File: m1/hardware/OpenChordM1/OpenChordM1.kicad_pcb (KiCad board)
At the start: 2 copper layers, 119 x 63.1 mm, 20 parts, among them J1 USB4105-GF-A, J2 SJ1-3523N, J3 SJ1-3523N, SW1 SW_Gateron_LP, SW10 EVQ-PUA02K, SW11 EVQ-PUA02K, SW2 SW_Gateron_LP, SW3 SW_Gateron_LP, SW4 SW_Gateron_LP, SW5 SW_Gateron_LP, SW6 SW_Gateron_LP, SW7 SW_Gateron_LP, SW8 SW_Gateron_LP, SW9 EVQ-PUA02K, U1 RP2040, U2 CT_Slider_Chev_3_74d5_15_noESD, U3 IQS572-BL-QNR, U4 AT42QT2120-XUR, U5 CT_Trackpad_7x7_37D75

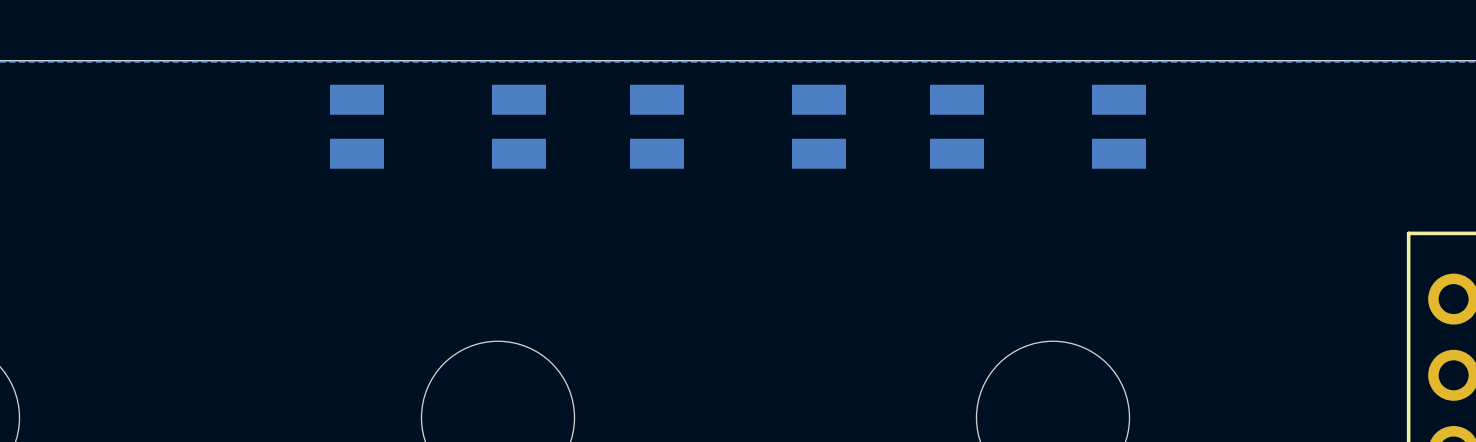
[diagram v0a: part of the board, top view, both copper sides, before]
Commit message: Lock M1 support BOM and add TLP2361 KiCad lib.
Document flash/crystal/LDO/ESD/MIDI IN recipe, replace H11L1 with TLP2361, and save current schematic/PCB progress before support-part placement.
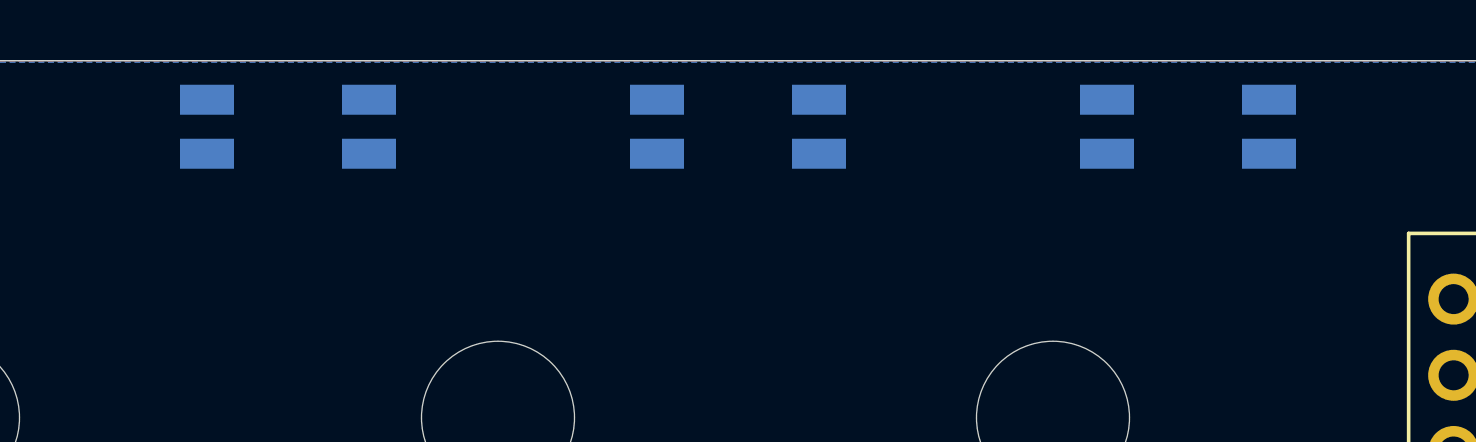
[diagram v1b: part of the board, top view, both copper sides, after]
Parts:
- moved SW10 5.00 mm to (160.0, 48.3)
- moved SW11 5.00 mm to (130.0, 48.3)
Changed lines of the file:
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@@
 	(footprint "oc-btn:EVQ-PUA02K"
 		(layer "B.Cu")
-		(at 155 48.3)
+		(at 160 48.3)
 		(property "Reference" "SW10"
 			(at 0 4.9 0)
@@
 				(font
 					(size 1.27 1.27)
+					(thickness 0.15)
 				)
 				(justify mirror)
@@
 				(font
 					(size 1.27 1.27)
+					(thickness 0.15)
 				)
 				(justify mirror)
@@
 	(footprint "oc-btn:EVQ-PUA02K"
 		(layer "B.Cu")
-		(at 135 48.3)
+		(at 130 48.3)
 		(property "Reference" "SW11"
 			(at 0 4.9 0)
@@
 				(font
 					(size 1.27 1.27)
+					(thickness 0.15)
 				)
 				(justify mirror)

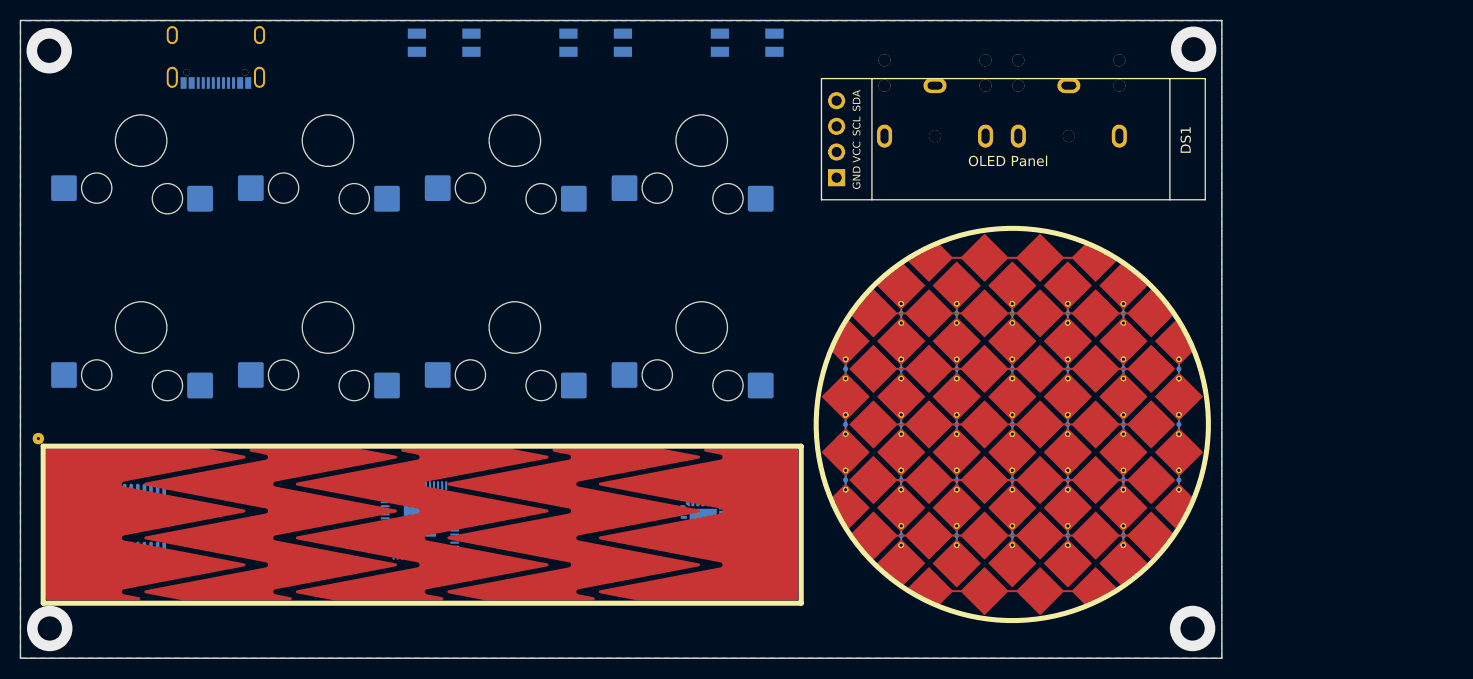
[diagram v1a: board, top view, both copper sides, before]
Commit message: Schematic and PCB update, hardware selections
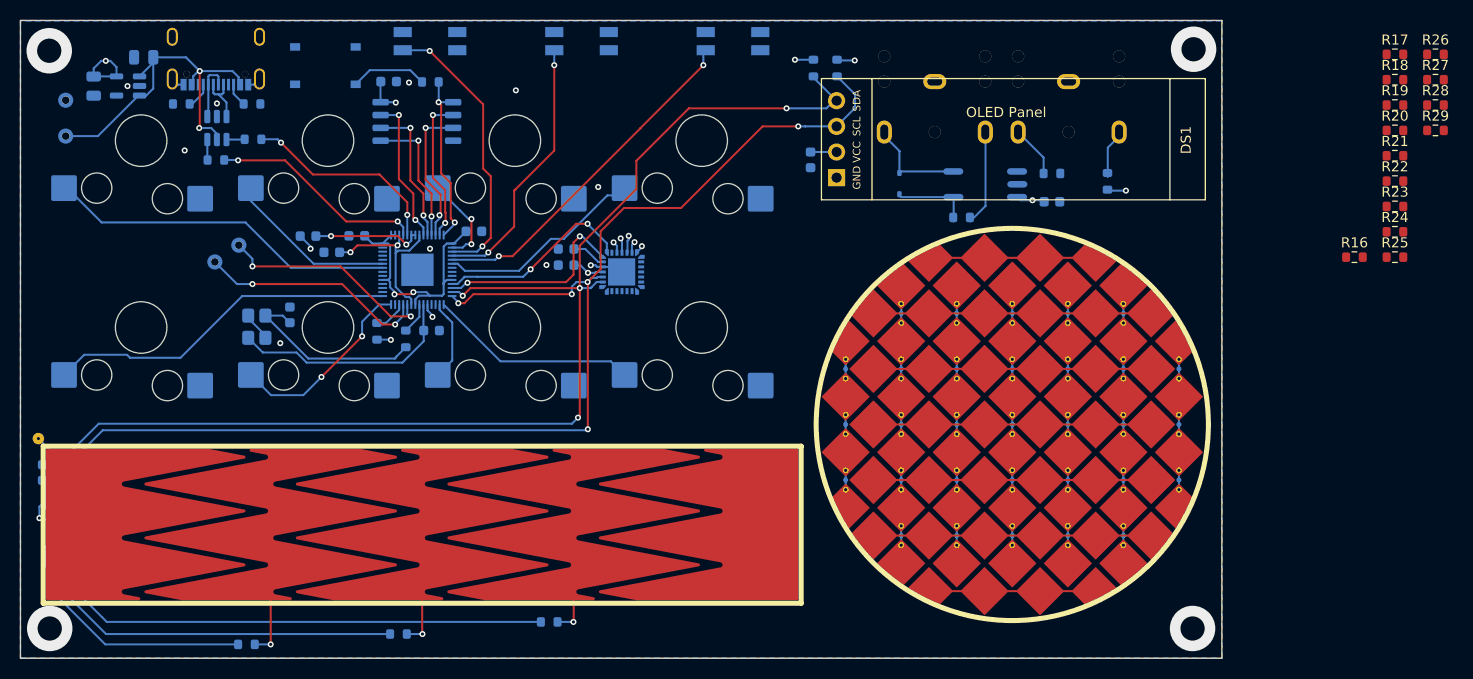
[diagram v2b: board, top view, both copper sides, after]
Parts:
- added C1: 100nF, Capacitor_SMD:C_0603_1608Metric, B.Cu at (124.5, 52.1)
- added C10: 10uF, Capacitor_SMD:C_0805_2012Metric, B.Cu at (100.2, 49.8)
- added C11: 10uF, Capacitor_SMD:C_0805_2012Metric, B.Cu at (95.3, 52.6)
- added C12: 15pF, Capacitor_SMD:C_0603_1608Metric, B.Cu at (128.8, 76.8)
- added C13: 15pF, Capacitor_SMD:C_0603_1608Metric, B.Cu at (114.7, 75.2)
- added C14: 100nF, Capacitor_SMD:C_0603_1608Metric, B.Cu at (166.3, 59.9)
- added C2: 100nF, Capacitor_SMD:C_0603_1608Metric, B.Cu at (142.1, 70.3)
- added C3: 100nF, Capacitor_SMD:C_0603_1608Metric, B.Cu at (90.2, 90.9)
- added C4: 100nF, Capacitor_SMD:C_0603_1608Metric, B.Cu at (116.5, 67.5)
- added C5: 100nF, Capacitor_SMD:C_0603_1608Metric, B.Cu at (132.9, 67.0)
- added C6: 100nF, Capacitor_SMD:C_0603_1608Metric, B.Cu at (190.2, 64.0)
- added C7: 1uF, Capacitor_SMD:C_0603_1608Metric, B.Cu at (142.1, 68.7)
- added C8: 1uF, Capacitor_SMD:C_0603_1608Metric, B.Cu at (118.9, 69.0)
- added C9: 1uF, Capacitor_SMD:C_0603_1608Metric, B.Cu at (121.3, 67.4)
- added D1: 1N4148WS, Diode_SMD:D_SOD-323, B.Cu at (175.1, 62.3)
- added R1: 5.1k, Resistor_SMD:R_0603_1608Metric, B.Cu at (111.0, 54.4)
- added R10: 220, Resistor_SMD:R_0603_1608Metric, B.Cu at (181.2, 65.6)
- added R11: 10, Resistor_SMD:R_0603_1608Metric, B.Cu at (190.2, 61.2)
- added R12: 33, Resistor_SMD:R_0603_1608Metric, B.Cu at (195.7, 62.0)
- added R13: 10k, Resistor_SMD:R_0603_1608Metric, B.Cu at (110.4, 107.9)
- added R14: 10k, Resistor_SMD:R_0603_1608Metric, B.Cu at (125.5, 106.8)
- added R15: 10k, Resistor_SMD:R_0603_1608Metric, B.Cu at (140.4, 105.7)
- added R16: 1k, Resistor_SMD:R_0603_1608Metric, F.Cu at (220.1, 69.5)
- added R17: 1k, Resistor_SMD:R_0603_1608Metric, F.Cu at (224.1, 49.5)
- added R18: 1k, Resistor_SMD:R_0603_1608Metric, F.Cu at (224.1, 52.0)
- added R19: 1k, Resistor_SMD:R_0603_1608Metric, F.Cu at (224.1, 54.5)
- added R2: 5.1k, Resistor_SMD:R_0603_1608Metric, B.Cu at (104.0, 54.4)
- added R20: 1k, Resistor_SMD:R_0603_1608Metric, F.Cu at (224.1, 57.0)
- added R21: 1k, Resistor_SMD:R_0603_1608Metric, F.Cu at (224.1, 59.5)
- added R22: 1k, Resistor_SMD:R_0603_1608Metric, F.Cu at (224.1, 62.0)
- added R23: 1k, Resistor_SMD:R_0603_1608Metric, F.Cu at (224.1, 64.5)
- added R24: 1k, Resistor_SMD:R_0603_1608Metric, F.Cu at (224.1, 67.0)
- added R25: 1k, Resistor_SMD:R_0603_1608Metric, F.Cu at (224.1, 69.5)
- added R26: 1k, Resistor_SMD:R_0603_1608Metric, F.Cu at (228.1, 49.5)
- added R27: 1k, Resistor_SMD:R_0603_1608Metric, F.Cu at (228.1, 52.0)
- added R28: 1k, Resistor_SMD:R_0603_1608Metric, F.Cu at (228.1, 54.5)
- added R29: 1k, Resistor_SMD:R_0603_1608Metric, F.Cu at (228.1, 57.0)
- added R3: 22R, Resistor_SMD:R_0603_1608Metric, B.Cu at (107.4, 59.9)
- added R4: 22R, Resistor_SMD:R_0603_1608Metric, B.Cu at (111.1, 57.9)
- added R5: 1k, Resistor_SMD:R_0603_1608Metric, B.Cu at (128.6, 52.2)
- added R6: 10k, Resistor_SMD:R_0603_1608Metric, B.Cu at (123.3, 76.9)
- added R7: 1k, Resistor_SMD:R_0603_1608Metric, B.Cu at (126.2, 77.6)
- added R8: 4.7k, Resistor_SMD:R_0603_1608Metric, B.Cu at (166.6, 50.8)
- added R9: 4.7k, Resistor_SMD:R_0603_1608Metric, B.Cu at (168.9, 50.8)
- added SW13: TS-1187A-B-A-B, oc-btn:TS-1187A-B-A-B, B.Cu at (118.2, 50.6)
- added TP-GND1: TestPoint, TestPoint:TestPoint_Pad_D1.5mm, B.Cu at (92.5, 54.0)
- added TP-SWCLK1: TestPoint, TestPoint:TestPoint_Pad_D1.5mm, B.Cu at (109.7, 68.3)
- added TP-SWDIO1: TestPoint, TestPoint:TestPoint_Pad_D1.5mm, B.Cu at (107.3, 70.0)
- added TP-VBUS1: TestPoint, TestPoint:TestPoint_Pad_D1.5mm, B.Cu at (92.5, 57.5)
- added U6: W25Q16JVSSIQ, Package_SO:SOIC-8_5.3x5.3mm_P1.27mm, B.Cu at (127.3, 56.1)
- added U7: AP2112K-3.3TRG1, Package_TO_SOT_SMD:SOT-23-5, B.Cu at (98.7, 52.6)
- added U8: USBLC6-2SC6, Package_TO_SOT_SMD:SOT-23-6, B.Cu at (107.5, 56.8)
- added U9: TLP2361, oc-midi:TLP2361, B.Cu at (183.6, 62.3)
- added Y1: ABM8-272-T3, Crystal:Crystal_SMD_3225-4Pin_3.2x2.5mm, B.Cu at (111.5, 76.4)
- J2: value SJ1-3523N -> SJ1-3523N (OUT)
- J3: value SJ1-3523N -> SJ1-3523N (IN)
- moved U3 26.1 mm to (147.6, 71.0), turned to 0 degrees
- moved U1 24.8 mm to (127.3, 70.8)
- moved U4 6.02 mm to (93.4, 96.6)
- moved SW10 1.41 mm to (158.6, 48.1)
- moved SW11 1.41 mm to (128.6, 48.1)
- moved SW9 1.41 mm to (143.6, 48.1)
- moved J2 0.40 mm to (191.8, 54.7)
- moved J3 0.40 mm to (178.6, 54.7)
- moved J1 0.16 mm to (107.4, 50.1)
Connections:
- DS1 pad 1: unconnected-(DS1-GND-Pad1) -> GND
- DS1 pad 2: unconnected-(DS1-VCC-Pad2) -> +3.3V
- DS1 pad 3: unconnected-(DS1-SCL-Pad3) -> /GPIO11
- DS1 pad 4: unconnected-(DS1-SDA-Pad4) -> /GPIO10
- J1 pad 1: unconnected-(J1-EH-Pad1) -> GND
- J1 pad 2: unconnected-(J1-EH-Pad2) -> GND
- J1 pad 3: unconnected-(J1-EH-Pad3) -> GND
- J1 pad 4: unconnected-(J1-EH-Pad4) -> GND
- J1 pad A1: unconnected-(J1-GND-PadA1) -> GND
- J1 pad A12: unconnected-(J1-GND-PadA12) -> GND
- J1 pad A4: unconnected-(J1-VBUS-PadA4) -> VBUS
- J1 pad A5: unconnected-(J1-CC1-PadA5) -> Net-(J1-CC1)
- J1 pad A6: unconnected-(J1-DP1-PadA6) -> Net-(J1-DP1)
- J1 pad A7: unconnected-(J1-DN1-PadA7) -> Net-(J1-DN1)
- J1 pad A9: unconnected-(J1-VBUS-PadA9) -> VBUS
- J1 pad B1: unconnected-(J1-GND-PadB1) -> GND
- J1 pad B12: unconnected-(J1-GND-PadB12) -> GND
- J1 pad B4: unconnected-(J1-VBUS-PadB4) -> VBUS
- J1 pad B5: unconnected-(J1-CC2-PadB5) -> Net-(J1-CC2)
- J1 pad B6: unconnected-(J1-DP2-PadB6) -> Net-(J1-DP1)
- J1 pad B7: unconnected-(J1-DN2-PadB7) -> Net-(J1-DN1)
- J1 pad B9: unconnected-(J1-VBUS-PadB9) -> VBUS
- J2 pad 1: unconnected-(J2-Sleeve-Pad1) -> GND
- J2 pad 2: unconnected-(J2-Tip-Pad2) -> Net-(J2-Tip)
- J2 pad 3: unconnected-(J2-Ring-Pad3) -> Net-(J2-Ring)
- J3 pad 1: unconnected-(J3-Sleeve-Pad1) -> GND
- J3 pad 2: unconnected-(J3-Tip-Pad2) -> Net-(J3-Tip)
- J3 pad 3: unconnected-(J3-Ring-Pad3) -> Net-(D1-A)
- SW1 pad 1: unconnected-(SW1-Pad1) -> /GPIO24
- SW1 pad 2: unconnected-(SW1-Pad2) -> GND
- SW10 pad 1: unconnected-(SW10-A-Pad1) -> GND
- SW10 pad 3: unconnected-(SW10-B-Pad3) -> /GPIO3
- SW11 pad 1: unconnected-(SW11-A-Pad1) -> GND
- SW11 pad 3: unconnected-(SW11-B-Pad3) -> /GPIO1
- SW2 pad 1: unconnected-(SW2-Pad1) -> /GPIO18
- SW2 pad 2: unconnected-(SW2-Pad2) -> GND
- SW3 pad 1: unconnected-(SW3-Pad1) -> /GPIO25
- SW3 pad 2: unconnected-(SW3-Pad2) -> GND
- SW4 pad 1: unconnected-(SW4-Pad1) -> /GPIO17
- SW4 pad 2: unconnected-(SW4-Pad2) -> GND
- SW5 pad 1: unconnected-(SW5-Pad1) -> /GPIO0
- SW5 pad 2: unconnected-(SW5-Pad2) -> GND
- SW6 pad 1: unconnected-(SW6-Pad1) -> /GPIO13
- SW6 pad 2: unconnected-(SW6-Pad2) -> GND
- SW7 pad 1: unconnected-(SW7-Pad1) -> /GPIO4
- SW7 pad 2: unconnected-(SW7-Pad2) -> GND
- SW8 pad 1: unconnected-(SW8-Pad1) -> /GPIO12
- SW8 pad 2: unconnected-(SW8-Pad2) -> GND
- SW9 pad 1: unconnected-(SW9-A-Pad1) -> GND
- SW9 pad 3: unconnected-(SW9-B-Pad3) -> /GPIO2
- U1 pad 1: Net-(U1-IOVDD-Pad1) -> +3.3V
- U1 pad 10: Net-(U1-IOVDD-Pad1) -> +3.3V
- U1 pad 11: unconnected-(U1-GPIO8-Pad11) -> /GPIO8
- U1 pad 12: unconnected-(U1-GPIO9-Pad12) -> /GPIO9
- U1 pad 13: unconnected-(U1-GPIO10-Pad13) -> /GPIO10
- U1 pad 14: unconnected-(U1-GPIO11-Pad14) -> /GPIO11
- U1 pad 15: unconnected-(U1-GPIO12-Pad15) -> /GPIO12
- U1 pad 16: unconnected-(U1-GPIO13-Pad16) -> /GPIO13
- U1 pad 17: unconnected-(U1-GPIO14-Pad17) -> /GPIO14
- U1 pad 18: unconnected-(U1-GPIO15-Pad18) -> /GPIO15
- U1 pad 19: unconnected-(U1-TESTEN-Pad19) -> GND
- U1 pad 2: unconnected-(U1-GPIO0-Pad2) -> /GPIO0
- U1 pad 20: unconnected-(U1-XIN-Pad20) -> Net-(U1-XIN)
- U1 pad 21: unconnected-(U1-XOUT-Pad21) -> Net-(U1-XOUT)
- U1 pad 22: Net-(U1-IOVDD-Pad1) -> +3.3V
- U1 pad 23: Net-(U1-DVDD-Pad23) -> Net-(U1-VREG_VOUT)
- U1 pad 24: unconnected-(U1-SWCLK-Pad24) -> Net-(U1-SWCLK)
- U1 pad 25: unconnected-(U1-SWDIO-Pad25) -> Net-(U1-SWDIO)
- U1 pad 26: unconnected-(U1-RUN-Pad26) -> Net-(U1-RUN)
- U1 pad 27: unconnected-(U1-GPIO16-Pad27) -> /GPIO16
- U1 pad 28: unconnected-(U1-GPIO17-Pad28) -> /GPIO17
- U1 pad 29: unconnected-(U1-GPIO18-Pad29) -> /GPIO18
- U1 pad 3: unconnected-(U1-GPIO1-Pad3) -> /GPIO1
- U1 pad 30: unconnected-(U1-GPIO19-Pad30) -> /GPIO19
- U1 pad 31: unconnected-(U1-GPIO20-Pad31) -> /GPIO20
- U1 pad 32: unconnected-(U1-GPIO21-Pad32) -> /GPIO21
- U1 pad 33: Net-(U1-IOVDD-Pad1) -> +3.3V
- U1 pad 34: unconnected-(U1-GPIO22-Pad34) -> /GPIO22
- U1 pad 35: unconnected-(U1-GPIO23-Pad35) -> /GPIO23
- U1 pad 36: unconnected-(U1-GPIO24-Pad36) -> /GPIO24
- U1 pad 37: unconnected-(U1-GPIO25-Pad37) -> /GPIO25
- U1 pad 4: unconnected-(U1-GPIO2-Pad4) -> /GPIO2
- U1 pad 42: Net-(U1-IOVDD-Pad1) -> +3.3V
- U1 pad 43: unconnected-(U1-ADC_AVDD-Pad43) -> +3.3V
- U1 pad 44: unconnected-(U1-VREG_VIN-Pad44) -> +3.3V
- U1 pad 45: unconnected-(U1-VREG_VOUT-Pad45) -> Net-(U1-VREG_VOUT)
- U1 pad 46: unconnected-(U1-USB_DM-Pad46) -> /USB_DN
- U1 pad 47: unconnected-(U1-USB_DP-Pad47) -> /USB_DP
- U1 pad 48: unconnected-(U1-USB_VDD-Pad48) -> +3.3V
- U1 pad 49: Net-(U1-IOVDD-Pad1) -> +3.3V
- U1 pad 5: unconnected-(U1-GPIO3-Pad5) -> /GPIO3
- U1 pad 50: Net-(U1-DVDD-Pad23) -> Net-(U1-VREG_VOUT)
- U1 pad 51: unconnected-(U1-QSPI_SD3-Pad51) -> Net-(U1-QSPI_SD3)
- U1 pad 52: unconnected-(U1-QSPI_SCLK-Pad52) -> Net-(U1-QSPI_SCLK)
- U1 pad 53: unconnected-(U1-QSPI_SD0-Pad53) -> Net-(U1-QSPI_SD0)
- U1 pad 54: unconnected-(U1-QSPI_SD2-Pad54) -> Net-(U1-QSPI_SD2)
- U1 pad 55: unconnected-(U1-QSPI_SD1-Pad55) -> Net-(U1-QSPI_SD1)
- U1 pad 56: unconnected-(U1-~{QSPI_SS}-Pad56) -> Net-(U1-~{QSPI_SS})
- U1 pad 6: unconnected-(U1-GPIO4-Pad6) -> /GPIO4
- U1 pad 7: unconnected-(U1-GPIO5-Pad7) -> /GPIO5
- U1 pad 8: unconnected-(U1-GPIO6-Pad8) -> /GPIO6
- U1 pad 9: unconnected-(U1-GPIO7-Pad9) -> /GPIO7
- U2 pad 1: unconnected-(U2-E1-Pad1) -> Net-(U2-E1)
- U2 pad 2: unconnected-(U2-E2-Pad2) -> Net-(U2-E2)
- U2 pad 3: unconnected-(U2-E3-Pad3) -> Net-(U2-E3)
- U2 pad 4: unconnected-(U2-GND-Pad4) -> GND
- U2 pad 5: unconnected-(U2-GND-Pad5) -> GND
- U2 pad 6: unconnected-(U2-GND-Pad6) -> GND
- U3 pad 10: unconnected-(U3-Rx0-Pad10) -> Net-(U3-Rx0)
- U3 pad 11: unconnected-(U3-Rx1-Pad11) -> Net-(U3-Rx1)
- U3 pad 12: unconnected-(U3-Rx2-Pad12) -> Net-(U3-Rx2)
- U3 pad 13: unconnected-(U3-Rx3-Pad13) -> Net-(U3-Rx3)
- U3 pad 14: unconnected-(U3-Rx4-Pad14) -> Net-(U3-Rx4)
- U3 pad 15: unconnected-(U3-Rx5-Pad15) -> Net-(U3-Rx5)
- U3 pad 16: unconnected-(U3-Rx6-Pad16) -> Net-(U3-Rx6)
- U3 pad 18: unconnected-(U3-Tx0-Pad18) -> Net-(U3-Tx0)
- U3 pad 19: unconnected-(U3-Tx1-Pad19) -> Net-(U3-Tx1)
- U3 pad 2: unconnected-(U3-SDA-Pad2) -> /GPIO10
- U3 pad 20: unconnected-(U3-Tx2-Pad20) -> Net-(U3-Tx2)
- U3 pad 21: unconnected-(U3-Tx3-Pad21) -> Net-(U3-Tx3)
- U3 pad 22: unconnected-(U3-Tx4-Pad22) -> Net-(U3-Tx4)
- U3 pad 23: unconnected-(U3-Tx5-Pad23) -> Net-(U3-Tx5)
- U3 pad 24: unconnected-(U3-Tx6-Pad24) -> Net-(U3-Tx6)
- U3 pad 29: unconnected-(U3-EP-Pad29) -> GND
- U3 pad 3: unconnected-(U3-SCL-Pad3) -> /GPIO11
- U3 pad 4: unconnected-(U3-VDDHI-Pad4) -> +3.3V
- U3 pad 5: unconnected-(U3-VSS-Pad5) -> GND
- U3 pad 6: unconnected-(U3-VREG-Pad6) -> Net-(U3-VREG)
- U3 pad 7: unconnected-(U3-NRST-Pad7) -> /GPIO9
- U3 pad 8: unconnected-(U3-RDY-Pad8) -> /GPIO8
- U4 pad 10: unconnected-(U4-VSS-Pad10) -> GND
- U4 pad 11: unconnected-(U4-VDD-Pad11) -> +3.3V
- U4 pad 12: unconnected-(U4-MODE-Pad12) -> GND
- U4 pad 13: unconnected-(U4-SDA-Pad13) -> /GPIO10
- U4 pad 14: unconnected-(U4-~{RESET}-Pad14) -> +3.3V
- U4 pad 16: unconnected-(U4-SCL-Pad16) -> /GPIO11
- U4 pad 7: unconnected-(U4-KEY2/GPO0-Pad7) -> Net-(U4-KEY2/GPO0)
- U4 pad 8: unconnected-(U4-KEY1-Pad8) -> Net-(U4-KEY1)
- U4 pad 9: unconnected-(U4-KEY0-Pad9) -> Net-(U4-KEY0)
- U5 pad 1: unconnected-(U5-Rx1-Pad1) -> Net-(U5-Rx1)
- U5 pad 10: unconnected-(U5-Tx3-Pad10) -> Net-(U5-Tx3)
- U5 pad 11: unconnected-(U5-Tx4-Pad11) -> Net-(U5-Tx4)
- U5 pad 12: unconnected-(U5-Tx5-Pad12) -> Net-(U5-Tx5)
- U5 pad 13: unconnected-(U5-Tx6-Pad13) -> Net-(U5-Tx6)
- U5 pad 14: unconnected-(U5-Tx7-Pad14) -> Net-(U5-Tx7)
- U5 pad 2: unconnected-(U5-Rx2-Pad2) -> Net-(U5-Rx2)
- U5 pad 3: unconnected-(U5-Rx3-Pad3) -> Net-(U5-Rx3)
- U5 pad 4: unconnected-(U5-Rx4-Pad4) -> Net-(U5-Rx4)
- U5 pad 5: unconnected-(U5-Rx5-Pad5) -> Net-(U5-Rx5)
- U5 pad 6: unconnected-(U5-Rx6-Pad6) -> Net-(U5-Rx6)
- U5 pad 7: unconnected-(U5-Rx7-Pad7) -> Net-(U5-Rx7)
- U5 pad 8: unconnected-(U5-Tx1-Pad8) -> Net-(U5-Tx1)
- U5 pad 9: unconnected-(U5-Tx2-Pad9) -> Net-(U5-Tx2)
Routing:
- net /GPIO11: track 0.00 -> 127.2 mm, vias 0 -> 5
- net /GPIO10: track 0.00 -> 126.3 mm, vias 0 -> 4
- net +3.3V: track 0.00 -> 71.0 mm, vias 0 -> 13
- net Net-(U4-KEY2/GPO0): track 0.00 -> 50.9 mm
- net Net-(U4-KEY1): track 0.00 -> 37.5 mm
- net VBUS: track 0.00 -> 36.1 mm, vias 0 -> 3
- net /GPIO18: track 0.00 -> 35.0 mm
- net /GPIO24: track 0.00 -> 34.8 mm
- net /GPIO3: track 0.00 -> 34.4 mm, vias 0 -> 2
- net /GPIO1: track 0.00 -> 28.1 mm, vias 0 -> 2
- net /GPIO2: track 0.00 -> 26.6 mm, vias 0 -> 2
- net Net-(U4-KEY0): track 0.00 -> 23.8 mm
- net Net-(U1-XIN): track 0.00 -> 22.9 mm
- net Net-(U1-SWDIO): track 0.00 -> 22.7 mm, vias 0 -> 3
- net Net-(U1-SWCLK): track 0.00 -> 21.9 mm, vias 0 -> 3
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- added copper zone on In2.Cu, net +3.3V
- added copper zone on In1.Cu, net GND
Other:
- copper layers 2 -> 4

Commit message: Lock rev A to in-stock parts and sync the board docs.
Use EVQPUC02K side buttons and W25Q32JVSSIQ flash, and add the Hroparts USB-C library so J1 can leave the out-of-stock GCT connector.
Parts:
- removed J1: USB4105-GF-A, oc-usb:USB4105-GF-A
- added J4: TYPE-C-31-M-12, oc-usb:TYPE-C-31-M-12, B.Cu at (107.4, 50.2)
- added R30: 10k, Resistor_SMD:R_0603_1608Metric, B.Cu at (133.7, 52.2)
- C2: value 100nF -> 1uF
- R16, R17, R18, R19, R20, R21, R22, R23, R24, R25, R26, R27, R28, R29: moved to B.Cu
- SW10, SW11, SW9: value EVQ-PUA02K -> EVQPUC02K; footprint oc-btn:EVQ-PUA02K -> oc-btn:EVQPUC02K
- U6: value W25Q16JVSSIQ -> W25Q32JVSSIQ
- moved R29 84.2 mm to (146.0, 75.3), turned to -90 degrees
- moved R28 83.1 mm to (147.7, 75.3), turned to -90 degrees
- moved R27 82.1 mm to (149.4, 75.3), turned to -90 degrees
- moved R26 81.2 mm to (151.1, 75.3), turned to -90 degrees
- moved R23 70.9 mm to (153.4, 69.8)
- moved R24 70.9 mm to (153.4, 71.4)
- moved R25 70.8 mm to (153.4, 73.0)
- moved R21 69.0 mm to (166.2, 97.0)
- moved R20 67.7 mm to (164.7, 89.4), turned to -90 degrees
- moved R22 66.5 mm to (171.8, 103.0)
- moved R19 65.6 mm to (165.4, 83.8), turned to -90 degrees
- moved R18 63.6 mm to (166.2, 78.4), turned to -90 degrees
- moved R17 60.6 mm to (168.1, 72.6)
- moved R16 45.6 mm to (174.6, 67.1)
- moved R2 0.23 mm to (104.0, 54.6), turned to 0 degrees
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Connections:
- R11 pad 2: unconnected-(R11-Pad2) -> /GPIO0
- R2 pad 1: Net-(J1-CC1) -> GND
- R2 pad 2: GND -> Net-(J4-CC1)
- SW10 pad 3: /GPIO3 -> /GPIO5
- SW11 pad 3: /GPIO1 -> /GPIO3
- SW5 pad 1: /GPIO0 -> /GPIO2
- SW7 pad 1: /GPIO4 -> /GPIO6
- SW9 pad 3: /GPIO2 -> /GPIO4
- U9 pad 5: unconnected-(U9-VO-Pad5) -> /GPIO1
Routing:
- net Net-(U5-Tx7): track 0.00 -> 86.5 mm, vias 0 -> 2
- net Net-(U5-Tx6): track 0.00 -> 77.3 mm, vias 0 -> 2
- net Net-(U5-Tx5): track 0.00 -> 70.0 mm, vias 0 -> 2
- net /GPIO0: track 9.15 -> 73.9 mm
- net Net-(U5-Tx4): track 0.00 -> 61.7 mm, vias 0 -> 2
- net Net-(U3-Rx6): track 0.00 -> 51.5 mm
- net Net-(U3-Rx5): track 0.00 -> 42.8 mm
- net /GPIO1: track 28.1 -> 69.0 mm
- net /GPIO5: track 0.00 -> 34.8 mm, vias 0 -> 2
- net Net-(U3-Rx4): track 0.77 -> 35.0 mm, vias 1 -> 0
- net Net-(U3-Rx3): track 1.16 -> 31.3 mm, vias 1 -> 0
- net Net-(U3-Rx0): track 1.16 -> 29.9 mm, vias 1 -> 0
- net Net-(U5-Tx3): track 0.00 -> 28.7 mm, vias 0 -> 2
- net Net-(U3-Rx2): track 1.75 -> 27.9 mm, vias 1 -> 0
- net Net-(U3-Rx1): track 1.48 -> 24.7 mm, vias 1 -> 0
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
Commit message: Lock Hroparts USB-C as J1, qty-5 order carts, and JLCPCB gerbers.
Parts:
- renumbered J4 to J1
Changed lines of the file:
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@@
 			(outputformat 1)
 			(mirror no)
-			(drillshape 1)
+			(drillshape 0)
 			(scaleselection 1)
 			(outputdirectory "")
@@
 			(layers "B.Cu" "B.Mask" "B.Paste")
 			(roundrect_rratio 0.25)
-			(net "Net-(J4-DN1)")
+			(net "Net-(J1-DN1)")
 			(pinfunction "I/O1_1")
 			(pintype "passive")
@@
 			(layers "B.Cu" "B.Mask" "B.Paste")
 			(roundrect_rratio 0.25)
-			(net "Net-(J4-DP1)")
+			(net "Net-(J1-DP1)")
 			(pinfunction "I/O2_3")
 			(pintype "passive")
@@
 			(layers "B.Cu" "B.Mask" "B.Paste")
 			(roundrect_rratio 0.25)
-			(net "Net-(J4-CC1)")
+			(net "Net-(J1-CC1)")
 			(pintype "passive")
 		)
@@
 			(layers "B.Cu" "B.Mask" "B.Paste")
 			(roundrect_rratio 0.25)
-			(net "Net-(J4-CC2)")
+			(net "Net-(J1-CC2)")
 			(pintype "passive")
 		)
@@
 		(layer "B.Cu")
 		(at 107.39 50.21)
-		(property "Reference" "J4"
+		(property "Reference" "J1"
 			(at 0 6.474 0)
 			(layer "B.SilkS")
@@
 		)
 		(property "LCSC Part" "C165948"
-			(at 0 0 0)
+			(at 0.09 -2.04 0)
 			(layer "B.Fab")
 			(effects
@@
 			(size 0.3 1.3)
 			(layers "B.Cu" "B.Mask" "B.Paste")
-			(net "Net-(J4-CC1)")
+			(net "Net-(J1-CC1)")
 			(pinfunction "CC1_A5")
 			(pintype "unspecified")
@@
 			(size 0.3 1.3)
 			(layers "B.Cu" "B.Mask" "B.Paste")
-			(net "Net-(J4-DP1)")
+			(net "Net-(J1-DP1)")
 			(pinfunction "DP1_A6")
 			(pintype "unspecified")
@@
 			(size 0.3 1.3)
 			(layers "B.Cu" "B.Mask" "B.Paste")
-			(net "Net-(J4-DN1)")
+			(net "Net-(J1-DN1)")
 			(pinfunction "DN1_A7")
 			(pintype "unspecified")
@@
 			(size 0.3 1.3)
 			(layers "B.Cu" "B.Mask" "B.Paste")
-			(net "unconnected-(J4-SBU1-PadA8)")
+			(net "unconnected-(J1-SBU1-PadA8)")
 			(pinfunction "SBU1_A8")
 			(pintype "unspecified+no_connect")
@@
 			(size 0.3 1.3)
 			(layers "B.Cu" "B.Mask" "B.Paste")
-			(net "Net-(J4-CC2)")
+			(net "Net-(J1-CC2)")
 			(pinfunction "CC2_B5")
 			(pintype "unspecified")
@@
 			(size 0.3 1.3)
 			(layers "B.Cu" "B.Mask" "B.Paste")
-			(net "Net-(J4-DP1)")
+			(net "Net-(J1-DP1)")
 			(pinfunction "DP2_B6")
 			(pintype "unspecified")
@@
 			(size 0.3 1.3)
 			(layers "B.Cu" "B.Mask" "B.Paste")
-			(net "Net-(J4-DN1)")
+			(net "Net-(J1-DN1)")
 			(pinfunction "DN2_B7")
 			(pintype "unspecified")
@@
 			(size 0.3 1.3)
 			(layers "B.Cu" "B.Mask" "B.Paste")
-			(net "unconnected-(J4-SBU2-PadB8)")
+			(net "unconnected-(J1-SBU2-PadB8)")
 			(pinfunction "SBU2_B8")
 			(pintype "unspecified+no_connect")
@@
 	)
 	(segment
-		(start 110.15 54.365)
-		(end 109.15 53.365)
+		(start 110.135 54.56)
+		(end 109.129848 53.554848)
 		(width 0.2)
 		(layer "B.Cu")
-		(net "Net-(J4-CC2)")
+		(net "Net-(J1-CC2)")
 	)
 	(segment
-		(start 109.15 53.365)
-		(end 109.15 52.455)
+		(start 109.129848 53.554848)
+		(end 109.129848 52.68)
 		(width 0.2)
 		(layer "B.Cu")
-		(net "Net-(J4-CC2)")
+		(net "Net-(J1-CC2)")
 	)
 	(segment
@@
 		(width 0.2)
 		(layer "B.Cu")
-		(net "Net-(J4-DP1)")
+		(net "Net-(J1-DP1)")
 	)
 	(segment
@@
 		(width 0.2)
 		(layer "B.Cu")
-		(net "Net-(J4-DP1)")
+		(net "Net-(J1-DP1)")
 	)
 	(segment
@@
 		(width 0.2)
 		(layer "B.Cu")
-		(net "Net-(J4-DP1)")
+		(net "Net-(J1-DP1)")
 	)
 	(segment
@@
 		(width 0.2)
 		(layer "B.Cu")
-		(net "Net-(J4-DP1)")
+		(net "Net-(J1-DP1)")
 	)
 	(segment
@@
 		(width 0.2)
 		(layer "B.Cu")
-		(net "Net-(J4-DP1)")
+		(net "Net-(J1-DP1)")
 	)
 	(segment
@@
 		(width 0.2)
 		(layer "B.Cu")
-		(net "Net-(J4-DP1)")
+		(net "Net-(J1-DP1)")
 	)
 	(segment
@@
 		(width 0.2)
 		(layer "B.Cu")
-		(net "Net-(J4-DP1)")
+		(net "Net-(J1-DP1)")
 	)
 	(segment
@@
 		(width 0.2)
 		(layer "B.Cu")
-		(net "Net-(J4-DP1)")
+		(net "Net-(J1-DP1)")
 	)
 	(segment
@@
 		(width 0.2)
 		(layer "B.Cu")
-		(net "Net-(J4-DN1)")
+		(net "Net-(J1-DN1)")
 	)
 	(segment
@@
 		(width 0.2)
 		(layer "B.Cu")
-		(net "Net-(J4-DN1)")
+		(net "Net-(J1-DN1)")
 	)
 	(segment
@@
 		(width 0.2)
 		(layer "B.Cu")
-		(net "Net-(J4-DN1)")
+		(net "Net-(J1-DN1)")
 	)
 	(segment
@@
 		(width 0.2)
 		(layer "B.Cu")
-		(net "Net-(J4-DN1)")
+		(net "Net-(J1-DN1)")
 	)
 	(segment
@@
 		(width 0.2)
 		(layer "B.Cu")
-		(net "Net-(J4-DN1)")
+		(net "Net-(J1-DN1)")
 	)
 	(segment
@@
 		(width 0.2)
 		(layer "B.Cu")
-		(net "Net-(J4-DN1)")
+		(net "Net-(J1-DN1)")
 	)
 	(segment
@@
 		(width 0.2)
 		(layer "B.Cu")
-		(net "Net-(J4-DN1)")
+		(net "Net-(J1-DN1)")
 	)
 	(segment
@@
 		(width 0.2)
 		(layer "B.Cu")
-		(net "Net-(J4-CC1)")
+		(net "Net-(J1-CC1)")
 	)
 	(segment
@@
 		(width 0.2)
 		(layer "B.Cu")
-		(net "Net-(J4-CC1)")
+		(net "Net-(J1-CC1)")
 	)
 	(segment
@@
 		(width 0.2)
 		(layer "B.Cu")
-		(net "Net-(J4-CC1)")
+		(net "Net-(J1-CC1)")
 	)
 	(zone
